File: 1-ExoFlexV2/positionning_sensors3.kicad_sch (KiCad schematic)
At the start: 31 parts, among them J107 Jumper, J108 Jumper, J109 Jumper, U79 COMP, U80 COMP, U81 COMP, U82 AND Gate, U83 AND Gate, U84 Inverter

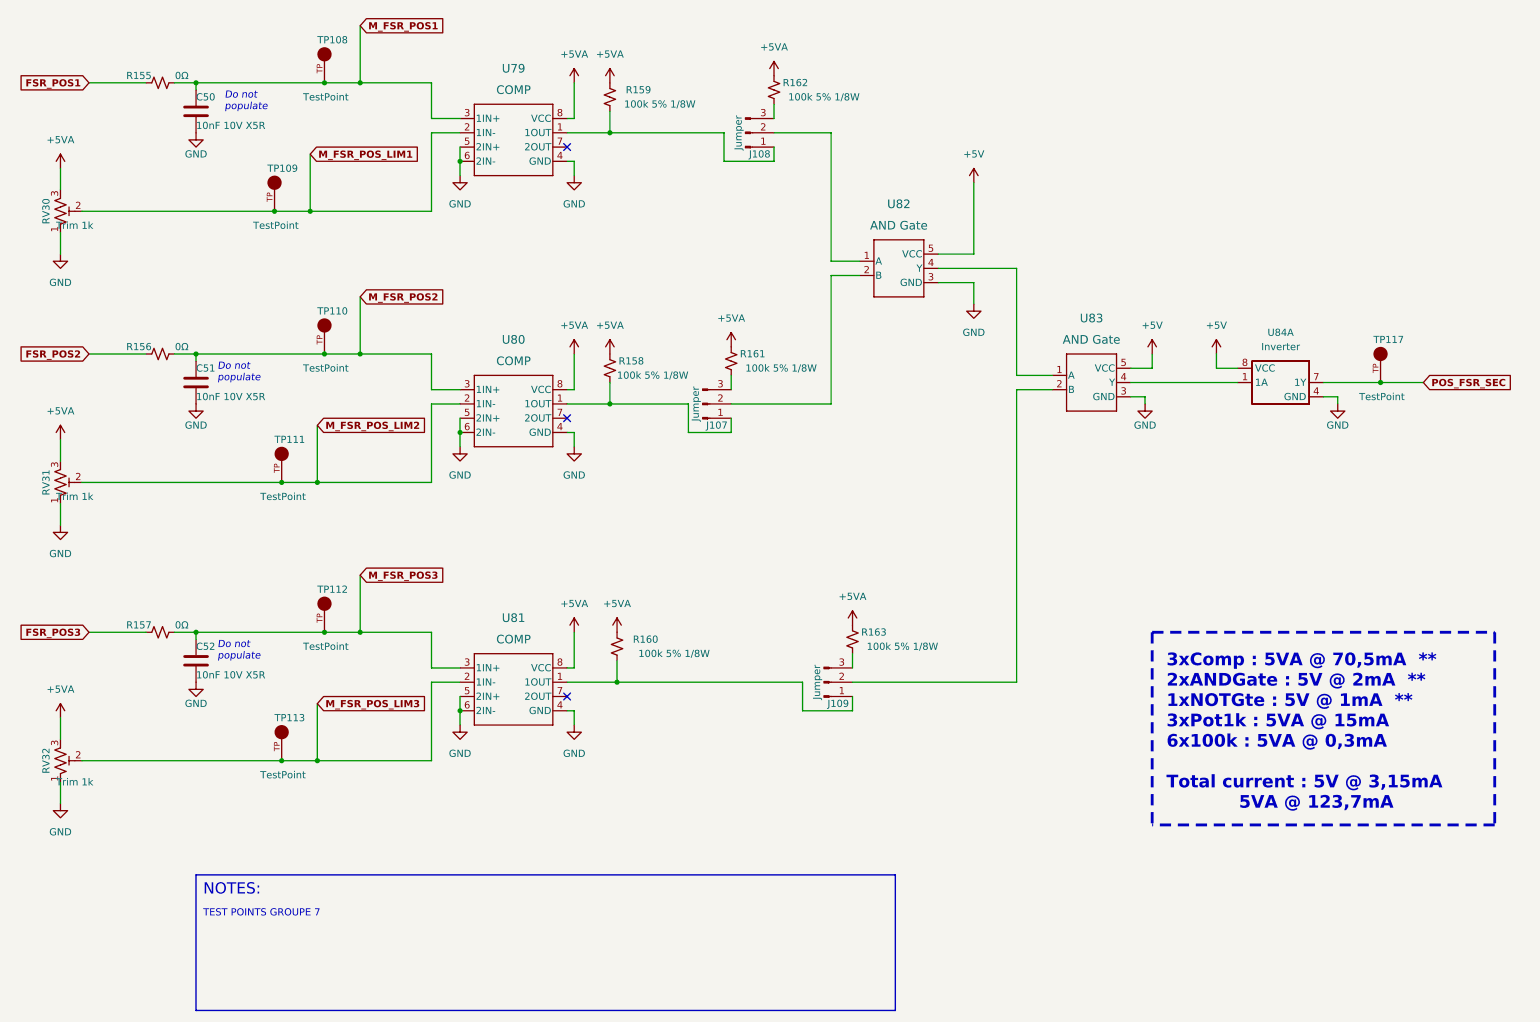
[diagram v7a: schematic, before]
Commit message: Finalisation schéma FIN
- Changement des uméro pour les inverseurs
- Changement des connecteur et début de placement
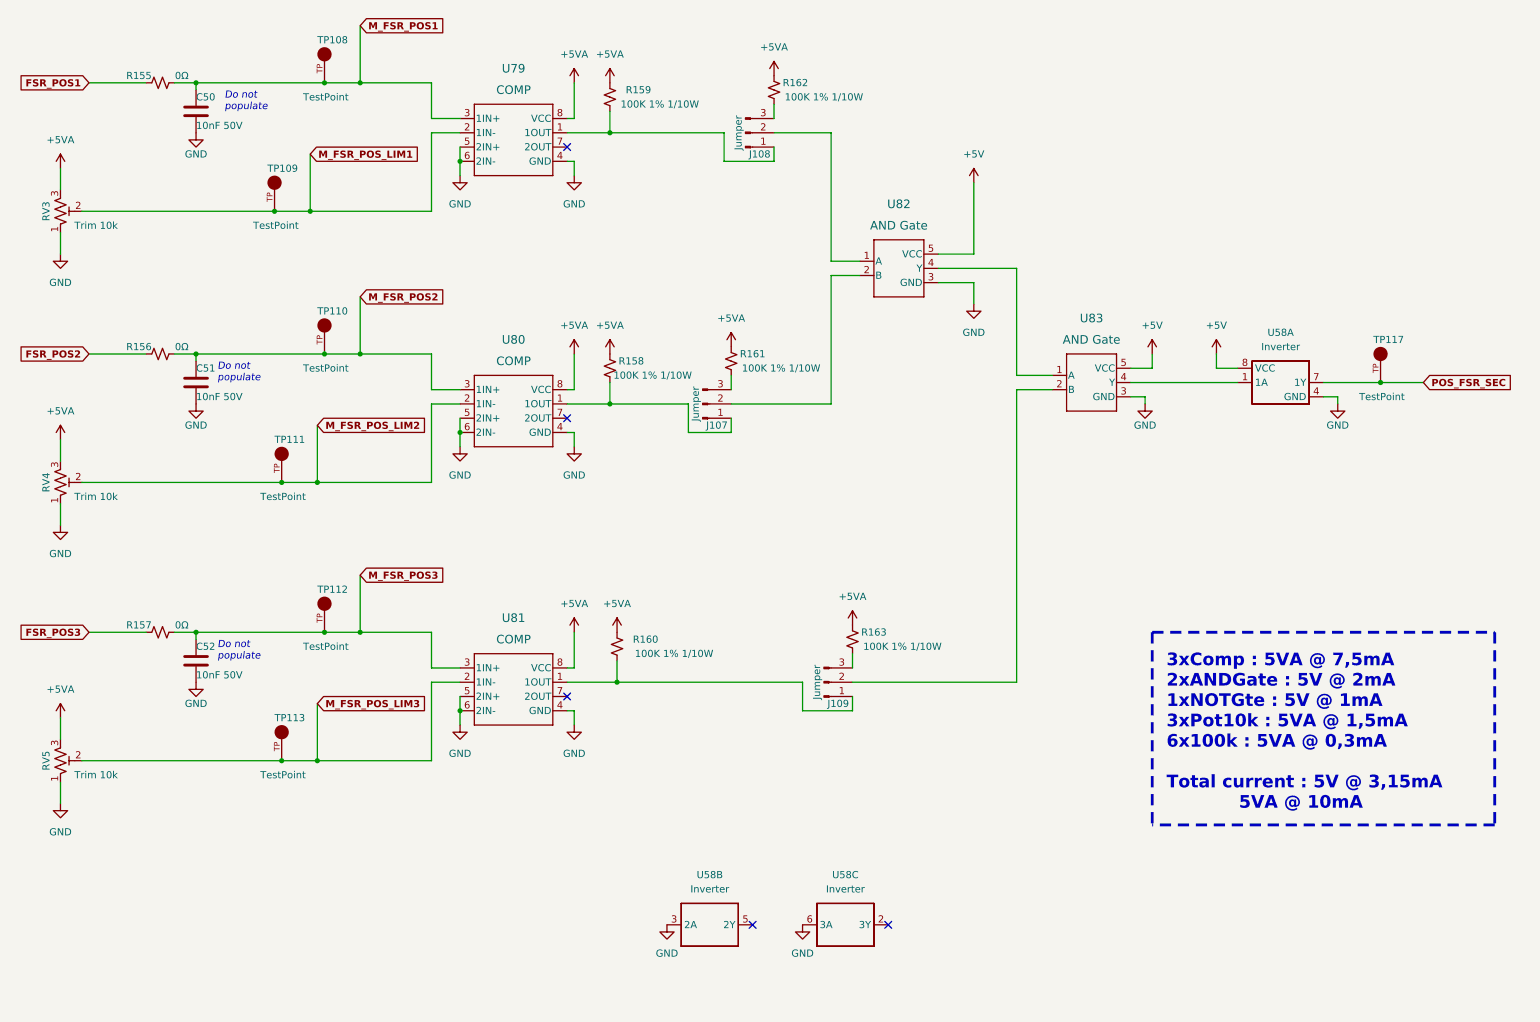
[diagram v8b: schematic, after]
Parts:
- removed RV30, RV31, RV32: Trim 1k, FootPrint:TRIM_3362P-1-102LF, symbol Device:R_Potentiometer_Trim_US
- removed U84: Inverter, FootPrint:SN74LVC3G14DCUT, symbol SymLib:SN74LVC3G14DCUT_V2
- added RV3, RV4, RV5: Trim 10k, FootPrint:TRIM_3362P-1-103LF, symbol Device:R_Potentiometer_Trim_US
- added U58: Inverter, FootPrint:SN74LVC3G14DCUT, symbol SymLib:SN74LVC3G14DCUT_V2
- C50, C51, C52: value 10nF 10V X5R -> 10nF 50V; footprint Capacitor_SMD:C_0603_1608Metric -> Capacitor_SMD:C_0805_2012Metric; DESCRIPTION 10000 pF ±5% 10V Ceramic Capacitor U2J 0603 (1608 Metric) -> 10000 pF ±5% 50V Ceramic Capacitor C0G, NP0 0805 (2012 Metr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; PACKAGE 0603 (1608 Metric) -> 0805 (2012 Metric); PART NUMBER GRM1857U1A103JA44D -> GRM2195C1H103JA01D
- R158, R159, R160, R161, R162, R163: value 100k 5% 1/8W -> 100K 1% 1/10W; footprint Resistor_SMD:R_0805_2012Metric -> Resistor_SMD:R_0603_1608Metric; DESCRIPTION 100 kOhms ±5% 0.125W, 1/8W Chip Resistor 0805 (2012 Metric)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 -> 100 kOhms ±1% 0.1W, 1/10W Chip Resistor 0603 (1608 Metric) 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; PACKAGE 0805 (2012 Metric) -> 0603 (1608 Metric); PART NUMBER ERJ-6GEYJ104V -> ERJ-3EKF1003V
- TP108, TP109, TP110, TP111, TP112, TP113, TP117: NOTES (none) -> DO NOT POPULATE; PURCHASE-URL https://pricing.snapeda.com/search/part/5005/?ref=eda -> (none)
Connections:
- net +5V: now also U58.8 (VCC)
- net +5VA: now also RV3.3, RV4.3, RV5.3
- net GND: now also RV3.1, RV4.1, RV5.1, U58.3 (2A), U58.4 (GND), U58.6 (3A)
- net M_FSR_POS_LIM1: now also RV3.2
- net M_FSR_POS_LIM2: now also RV4.2
- net M_FSR_POS_LIM3: now also RV5.2
- net POS_FSR_SEC: now also U58.7 (1Y)
- net at U83.4 (Y): now also U58.1 (1A)
- no-connect marks 3 -> 5
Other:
- note added: "3xComp : 5VA @ 7,5mA 2xANDGate : 5V @ 2mA 1xNOTGte : 5V @ 1mA 3xPot10k : 5VA @ 1,5mA 6x100k : 5VA @ 0,3mA Total current : 5V @ 3,15mA 5VA @ 10mA"
- note removed: "3xComp : 5VA @ 70,5mA ** 2xANDGate : 5V @ 2mA ** 1xNOTGte : 5V @ 1mA ** 3xPot1k : 5VA @ 15mA 6x100k : 5VA @ 0,3mA Total current : 5V @ 3,15mA 5VA @ 123,7mA"
- note removed: "NOTES:"
- note removed: "TEST POINTS GROUPE 7"
